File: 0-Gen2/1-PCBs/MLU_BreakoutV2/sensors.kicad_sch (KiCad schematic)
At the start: 6 parts, among them U2 MCP9808_MSOP, U3 MCP9808_MSOP, U4 BME280

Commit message: before restructure
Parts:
- renumbered R1 to R5, R2 to R6, R3 to R7, U2 to U3, U3 to U4, U4 to U5
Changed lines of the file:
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@@
 		(dnp no)
 		(fields_autoplaced yes)
-		(property "Reference" "#PWR021"
+		(property "Reference" "#PWR0145"
 			(at 93.472 59.182 0)
 			(effects
@@
 			(project "MLU_BreakoutV2"
 				(path "/55121ba7-5d22-4fe3-93aa-7f76d75b410c/9dab6a9b-c343-4374-86a4-2dd37d3a47bf"
-					(reference "#PWR021")
+					(reference "#PWR0145")
 					(unit 1)
 				)
@@
 		(dnp no)
 		(fields_autoplaced yes)
-		(property "Reference" "#PWR019"
+		(property "Reference" "#PWR0143"
 			(at 79.502 56.642 0)
 			(effects
@@
 			(project "MLU_BreakoutV2"
 				(path "/55121ba7-5d22-4fe3-93aa-7f76d75b410c/9dab6a9b-c343-4374-86a4-2dd37d3a47bf"
-					(reference "#PWR019")
+					(reference "#PWR0143")
 					(unit 1)
 				)
@@
 		(on_board yes)
 		(dnp no)
-		(property "Reference" "R2"
+		(property "Reference" "R6"
 			(at 126.238 42.6719 0)
 			(effects
@@
 			(project "MLU_BreakoutV2"
 				(path "/55121ba7-5d22-4fe3-93aa-7f76d75b410c/9dab6a9b-c343-4374-86a4-2dd37d3a47bf"
-					(reference "R2")
+					(reference "R6")
 					(unit 1)
 				)
@@
 		(on_board yes)
 		(dnp no)
-		(property "Reference" "#PWR012"
+		(property "Reference" "#PWR0138"
 			(at 43.18 30.988 0)
 			(effects
@@
 			(project "MLU_BreakoutV2"
 				(path "/55121ba7-5d22-4fe3-93aa-7f76d75b410c/9dab6a9b-c343-4374-86a4-2dd37d3a47bf"
-					(reference "#PWR012")
+					(reference "#PWR0138")
 					(unit 1)
 				)
@@
 		(dnp no)
 		(fields_autoplaced yes)
-		(property "Reference" "#PWR018"
+		(property "Reference" "#PWR0142"
 			(at 28.956 53.848 0)
 			(effects
@@
 			(project "MLU_BreakoutV2"
 				(path "/55121ba7-5d22-4fe3-93aa-7f76d75b410c/9dab6a9b-c343-4374-86a4-2dd37d3a47bf"
-					(reference "#PWR018")
+					(reference "#PWR0142")
 					(unit 1)
 				)
@@
 		(on_board yes)
 		(dnp no)
-		(property "Reference" "R3"
+		(property "Reference" "R7"
 			(at 73.406 45.2119 0)
 			(effects
@@
 			(project "MLU_BreakoutV2"
 				(path "/55121ba7-5d22-4fe3-93aa-7f76d75b410c/9dab6a9b-c343-4374-86a4-2dd37d3a47bf"
-					(reference "R3")
+					(reference "R7")
 					(unit 1)
 				)
@@
 		(dnp no)
 		(fields_autoplaced yes)
-		(property "Reference" "U2"
+		(property "Reference" "U3"
 			(at 59.944 33.5594 0)
 			(effects
@@
 			(project "MLU_BreakoutV2"
 				(path "/55121ba7-5d22-4fe3-93aa-7f76d75b410c/9dab6a9b-c343-4374-86a4-2dd37d3a47bf"
-					(reference "U2")
+					(reference "U3")
 					(unit 1)
 				)
@@
 		(on_board yes)
 		(dnp no)
-		(property "Reference" "U4"
+		(property "Reference" "U5"
 			(at 171.704 38.8619 0)
 			(effects
@@
 			(project "MLU_BreakoutV2"
 				(path "/55121ba7-5d22-4fe3-93aa-7f76d75b410c/9dab6a9b-c343-4374-86a4-2dd37d3a47bf"
-					(reference "U4")
+					(reference "U5")
 					(unit 1)
 				)
@@
 		(on_board yes)
 		(dnp no)
-		(property "Reference" "#PWR017"
+		(property "Reference" "#PWR0141"
 			(at 75.184 46.482 0)
 			(effects
@@
 			(project "MLU_BreakoutV2"
 				(path "/55121ba7-5d22-4fe3-93aa-7f76d75b410c/9dab6a9b-c343-4374-86a4-2dd37d3a47bf"
-					(reference "#PWR017")
+					(reference "#PWR0141")
 					(unit 1)
 				)
@@
 		(dnp no)
 		(fields_autoplaced yes)
-		(property "Reference" "#PWR022"
+		(property "Reference" "#PWR0146"
 			(at 159.512 61.722 0)
 			(effects
@@
 			(project "MLU_BreakoutV2"
 				(path "/55121ba7-5d22-4fe3-93aa-7f76d75b410c/9dab6a9b-c343-4374-86a4-2dd37d3a47bf"
-					(reference "#PWR022")
+					(reference "#PWR0146")
 					(unit 1)
 				)
@@
 		(dnp no)
 		(fields_autoplaced yes)
-		(property "Reference" "U3"
+		(property "Reference" "U4"
 			(at 110.236 33.8134 0)
 			(effects
@@
 			(project "MLU_BreakoutV2"
 				(path "/55121ba7-5d22-4fe3-93aa-7f76d75b410c/9dab6a9b-c343-4374-86a4-2dd37d3a47bf"
-					(reference "U3")
+					(reference "U4")
 					(unit 1)
 				)
@@
 		(on_board yes)
 		(dnp no)
-		(property "Reference" "#PWR09"
+		(property "Reference" "#PWR0137"
 			(at 159.766 28.702 0)
 			(effects
@@
 			(project "MLU_BreakoutV2"
 				(path "/55121ba7-5d22-4fe3-93aa-7f76d75b410c/9dab6a9b-c343-4374-86a4-2dd37d3a47bf"
-					(reference "#PWR09")
+					(reference "#PWR0137")
 					(unit 1)
 				)
@@
 		(on_board yes)
 		(dnp no)
-		(property "Reference" "#PWR014"
+		(property "Reference" "#PWR0140"
 			(at 128.016 43.942 0)
 			(effects
@@
 			(project "MLU_BreakoutV2"
 				(path "/55121ba7-5d22-4fe3-93aa-7f76d75b410c/9dab6a9b-c343-4374-86a4-2dd37d3a47bf"
-					(reference "#PWR014")
+					(reference "#PWR0140")
 					(unit 1)
 				)
@@
 		(on_board yes)
 		(dnp no)
-		(property "Reference" "R1"
+		(property "Reference" "R5"
 			(at 142.494 27.4319 0)
 			(effects
@@
 			(project "MLU_BreakoutV2"
 				(path "/55121ba7-5d22-4fe3-93aa-7f76d75b410c/9dab6a9b-c343-4374-86a4-2dd37d3a47bf"
-					(reference "R1")
+					(reference "R5")
 					(unit 1)
 				)
@@
 		(on_board yes)
 		(dnp no)
-		(property "Reference" "#PWR013"
+		(property "Reference" "#PWR0139"
 			(at 93.472 31.242 0)
 			(effects
@@
 			(project "MLU_BreakoutV2"
 				(path "/55121ba7-5d22-4fe3-93aa-7f76d75b410c/9dab6a9b-c343-4374-86a4-2dd37d3a47bf"
-					(reference "#PWR013")
+					(reference "#PWR0139")
 					(unit 1)
 				)
@@
 		(dnp no)
 		(fields_autoplaced yes)
-		(property "Reference" "#PWR020"
+		(property "Reference" "#PWR0144"
 			(at 43.18 58.928 0)
 			(effects
@@
 			(project "MLU_BreakoutV2"
 				(path "/55121ba7-5d22-4fe3-93aa-7f76d75b410c/9dab6a9b-c343-4374-86a4-2dd37d3a47bf"
-					(reference "#PWR020")
-					(unit 1)
-				)
+					(reference "#PWR0144")
+					(unit 1)
+				)

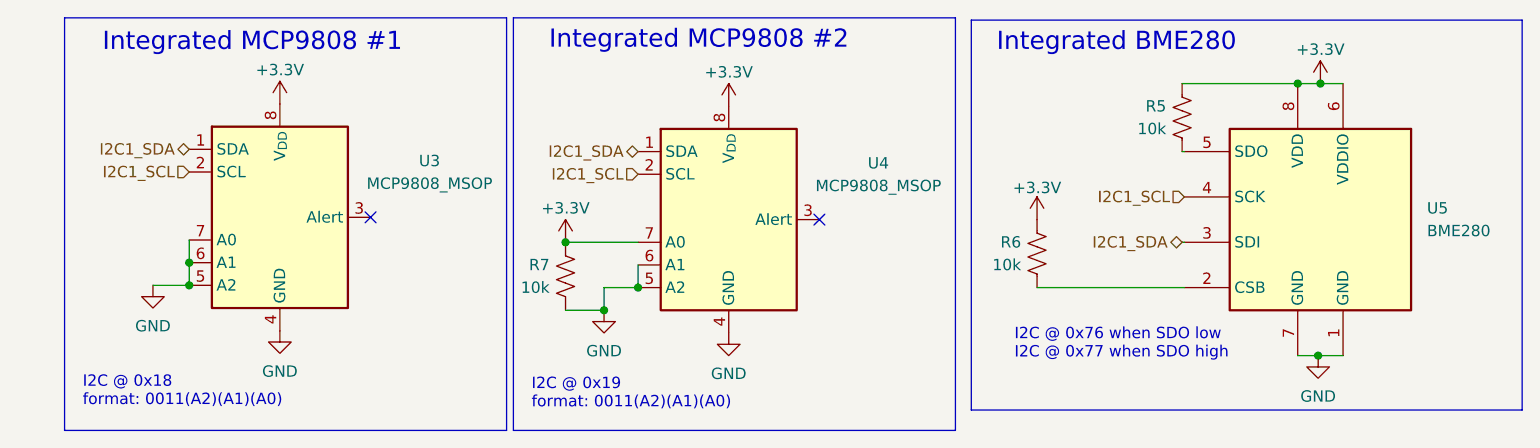
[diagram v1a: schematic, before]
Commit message: [bugfix] rescued footprints
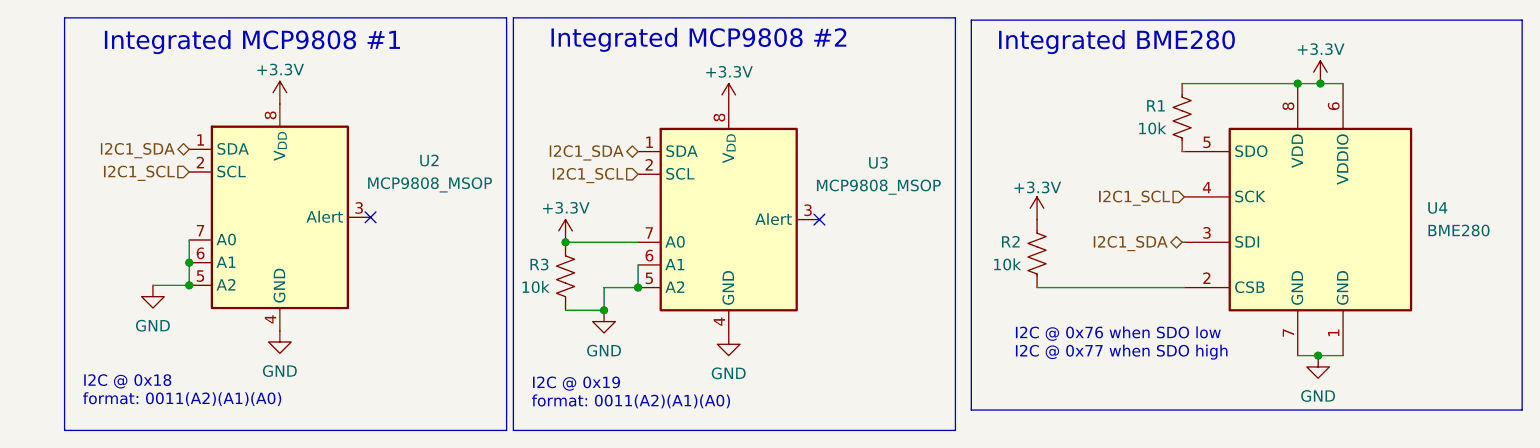
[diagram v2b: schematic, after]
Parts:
- renumbered R5 to R1, R6 to R2, R7 to R3, U3 to U2, U4 to U3, U5 to U4
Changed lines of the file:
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@@
 		(dnp no)
 		(fields_autoplaced yes)
-		(property "Reference" "#PWR0145"
+		(property "Reference" "#PWR021"
 			(at 93.472 59.182 0)
 			(effects
@@
 			(project "MLU_BreakoutV2"
 				(path "/55121ba7-5d22-4fe3-93aa-7f76d75b410c/9dab6a9b-c343-4374-86a4-2dd37d3a47bf"
-					(reference "#PWR0145")
+					(reference "#PWR021")
 					(unit 1)
 				)
@@
 		(dnp no)
 		(fields_autoplaced yes)
-		(property "Reference" "#PWR0143"
+		(property "Reference" "#PWR019"
 			(at 79.502 56.642 0)
 			(effects
@@
 			(project "MLU_BreakoutV2"
 				(path "/55121ba7-5d22-4fe3-93aa-7f76d75b410c/9dab6a9b-c343-4374-86a4-2dd37d3a47bf"
-					(reference "#PWR0143")
+					(reference "#PWR019")
 					(unit 1)
 				)
@@
 		(on_board yes)
 		(dnp no)
-		(property "Reference" "R6"
+		(property "Reference" "R2"
 			(at 126.238 42.6719 0)
 			(effects
@@
 			(project "MLU_BreakoutV2"
 				(path "/55121ba7-5d22-4fe3-93aa-7f76d75b410c/9dab6a9b-c343-4374-86a4-2dd37d3a47bf"
-					(reference "R6")
+					(reference "R2")
 					(unit 1)
 				)
@@
 		(on_board yes)
 		(dnp no)
-		(property "Reference" "#PWR0138"
+		(property "Reference" "#PWR012"
 			(at 43.18 30.988 0)
 			(effects
@@
 			(project "MLU_BreakoutV2"
 				(path "/55121ba7-5d22-4fe3-93aa-7f76d75b410c/9dab6a9b-c343-4374-86a4-2dd37d3a47bf"
-					(reference "#PWR0138")
+					(reference "#PWR012")
 					(unit 1)
 				)
@@
 		(dnp no)
 		(fields_autoplaced yes)
-		(property "Reference" "#PWR0142"
+		(property "Reference" "#PWR018"
 			(at 28.956 53.848 0)
 			(effects
@@
 			(project "MLU_BreakoutV2"
 				(path "/55121ba7-5d22-4fe3-93aa-7f76d75b410c/9dab6a9b-c343-4374-86a4-2dd37d3a47bf"
-					(reference "#PWR0142")
+					(reference "#PWR018")
 					(unit 1)
 				)
@@
 		(on_board yes)
 		(dnp no)
-		(property "Reference" "R7"
+		(property "Reference" "R3"
 			(at 73.406 45.2119 0)
 			(effects
@@
 			(project "MLU_BreakoutV2"
 				(path "/55121ba7-5d22-4fe3-93aa-7f76d75b410c/9dab6a9b-c343-4374-86a4-2dd37d3a47bf"
-					(reference "R7")
+					(reference "R3")
 					(unit 1)
 				)
@@
 		(dnp no)
 		(fields_autoplaced yes)
-		(property "Reference" "U3"
+		(property "Reference" "U2"
 			(at 59.944 33.5594 0)
 			(effects
@@
 			(project "MLU_BreakoutV2"
 				(path "/55121ba7-5d22-4fe3-93aa-7f76d75b410c/9dab6a9b-c343-4374-86a4-2dd37d3a47bf"
-					(reference "U3")
+					(reference "U2")
 					(unit 1)
 				)
@@
 		(on_board yes)
 		(dnp no)
-		(property "Reference" "U5"
+		(property "Reference" "U4"
 			(at 171.704 38.8619 0)
 			(effects
@@
 			(project "MLU_BreakoutV2"
 				(path "/55121ba7-5d22-4fe3-93aa-7f76d75b410c/9dab6a9b-c343-4374-86a4-2dd37d3a47bf"
-					(reference "U5")
+					(reference "U4")
 					(unit 1)
 				)
@@
 		(on_board yes)
 		(dnp no)
-		(property "Reference" "#PWR0141"
+		(property "Reference" "#PWR017"
 			(at 75.184 46.482 0)
 			(effects
@@
 			(project "MLU_BreakoutV2"
 				(path "/55121ba7-5d22-4fe3-93aa-7f76d75b410c/9dab6a9b-c343-4374-86a4-2dd37d3a47bf"
-					(reference "#PWR0141")
+					(reference "#PWR017")
 					(unit 1)
 				)
@@
 		(dnp no)
 		(fields_autoplaced yes)
-		(property "Reference" "#PWR0146"
+		(property "Reference" "#PWR022"
 			(at 159.512 61.722 0)
 			(effects
@@
 			(project "MLU_BreakoutV2"
 				(path "/55121ba7-5d22-4fe3-93aa-7f76d75b410c/9dab6a9b-c343-4374-86a4-2dd37d3a47bf"
-					(reference "#PWR0146")
+					(reference "#PWR022")
 					(unit 1)
 				)
@@
 		(dnp no)
 		(fields_autoplaced yes)
-		(property "Reference" "U4"
+		(property "Reference" "U3"
 			(at 110.236 33.8134 0)
 			(effects
@@
 			(project "MLU_BreakoutV2"
 				(path "/55121ba7-5d22-4fe3-93aa-7f76d75b410c/9dab6a9b-c343-4374-86a4-2dd37d3a47bf"
-					(reference "U4")
+					(reference "U3")
 					(unit 1)
 				)
@@
 		(on_board yes)
 		(dnp no)
-		(property "Reference" "#PWR0137"
+		(property "Reference" "#PWR09"
 			(at 159.766 28.702 0)
 			(effects
@@
 			(project "MLU_BreakoutV2"
 				(path "/55121ba7-5d22-4fe3-93aa-7f76d75b410c/9dab6a9b-c343-4374-86a4-2dd37d3a47bf"
-					(reference "#PWR0137")
+					(reference "#PWR09")
 					(unit 1)
 				)
@@
 		(on_board yes)
 		(dnp no)
-		(property "Reference" "#PWR0140"
+		(property "Reference" "#PWR014"
 			(at 128.016 43.942 0)
 			(effects
@@
 			(project "MLU_BreakoutV2"
 				(path "/55121ba7-5d22-4fe3-93aa-7f76d75b410c/9dab6a9b-c343-4374-86a4-2dd37d3a47bf"
-					(reference "#PWR0140")
+					(reference "#PWR014")
 					(unit 1)
 				)
@@
 		(on_board yes)
 		(dnp no)
-		(property "Reference" "R5"
+		(property "Reference" "R1"
 			(at 142.494 27.4319 0)
 			(effects
@@
 			(project "MLU_BreakoutV2"
 				(path "/55121ba7-5d22-4fe3-93aa-7f76d75b410c/9dab6a9b-c343-4374-86a4-2dd37d3a47bf"
-					(reference "R5")
+					(reference "R1")
 					(unit 1)
 				)
@@
 		(on_board yes)
 		(dnp no)
-		(property "Reference" "#PWR0139"
+		(property "Reference" "#PWR013"
 			(at 93.472 31.242 0)
 			(effects
@@
 			(project "MLU_BreakoutV2"
 				(path "/55121ba7-5d22-4fe3-93aa-7f76d75b410c/9dab6a9b-c343-4374-86a4-2dd37d3a47bf"
-					(reference "#PWR0139")
+					(reference "#PWR013")
 					(unit 1)
 				)
@@
 		(dnp no)
 		(fields_autoplaced yes)
-		(property "Reference" "#PWR0144"
+		(property "Reference" "#PWR020"
 			(at 43.18 58.928 0)
 			(effects
@@
 			(project "MLU_BreakoutV2"
 				(path "/55121ba7-5d22-4fe3-93aa-7f76d75b410c/9dab6a9b-c343-4374-86a4-2dd37d3a47bf"
-					(reference "#PWR0144")
-					(unit 1)
-				)
+					(reference "#PWR020")
+					(unit 1)
+				)
